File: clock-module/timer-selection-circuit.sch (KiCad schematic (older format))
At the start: 15 parts

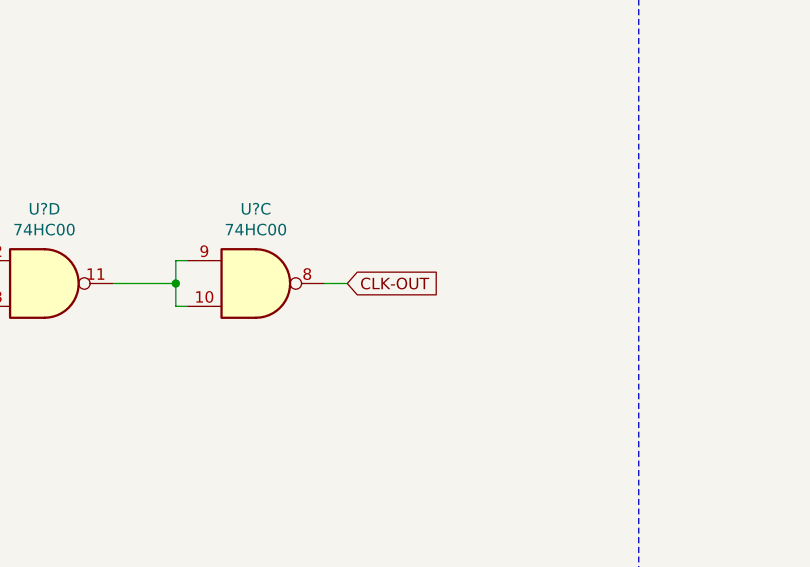
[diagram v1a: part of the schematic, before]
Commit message: Add clock inverter to clock-module, correct label directions
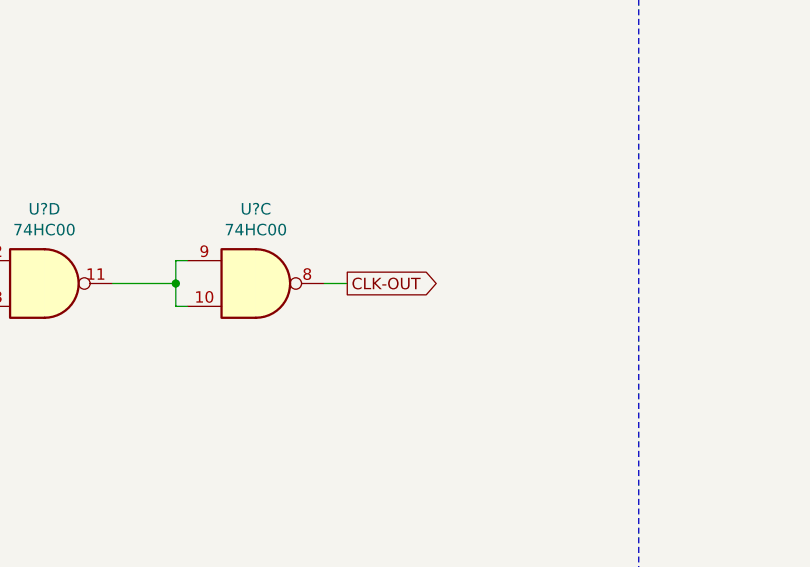
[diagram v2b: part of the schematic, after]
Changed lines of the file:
@@
 Text Notes 625  700  0    79   ~ 16
 Timer Selection Circuit
-Text GLabel 5700 2575 2    50   Input ~ 0
+Text GLabel 5700 2575 2    50   Output ~ 0
 CLK-OUT
 Wire Wire Line

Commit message: ERC complete on clock-module, add HLT connector
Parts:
- gave numbers to parts that had none: 7
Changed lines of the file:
@@
 	5000 2475 4950 2475
 $Comp
-L 74xx:74HC00 U?
+L 74xx:74HC00 U4
 U 3 1 5D440F0A
 P 5300 2575
-AR Path="/5D28C6D7/5D440F0A" Ref="U?"  Part="3"
+AR Path="/5D28C6D7/5D440F0A" Ref="U4"  Part="3"
 AR Path="/5D440F0A" Ref="U?"  Part="3"
-F 0 "U?" H 5300 2900 50  0000 C CNN
+F 0 "U4" H 5300 2900 50  0000 C CNN
 F 1 "74HC00" H 5300 2809 50  0000 C CNN
 F 2 "" H 5300 2575 50  0001 C CNN
@@
 $EndComp
 $Comp
-L 74xx:74HC00 U?
+L 74xx:74HC00 U4
 U 4 1 5D440F10
 P 4375 2575
-AR Path="/5D28C6D7/5D440F10" Ref="U?"  Part="4"
+AR Path="/5D28C6D7/5D440F10" Ref="U4"  Part="4"
 AR Path="/5D440F10" Ref="U?"  Part="4"
-F 0 "U?" H 4375 2900 50  0000 C CNN
+F 0 "U4" H 4375 2900 50  0000 C CNN
 F 1 "74HC00" H 4375 2809 50  0000 C CNN
 F 2 "" H 4375 2575 50  0001 C CNN
@@
 $EndComp
 $Comp
-L 74xx:74HC00 U?
+L 74xx:74HC00 U3
 U 2 1 5D440F16
 P 3575 2200
-AR Path="/5D28C6D7/5D440F16" Ref="U?"  Part="2"
+AR Path="/5D28C6D7/5D440F16" Ref="U3"  Part="2"
 AR Path="/5D440F16" Ref="U?"  Part="2"
-F 0 "U?" H 3575 2525 50  0000 C CNN
+F 0 "U3" H 3575 2525 50  0000 C CNN
 F 1 "74HC00" H 3575 2434 50  0000 C CNN
 F 2 "" H 3575 2200 50  0001 C CNN
@@
 $EndComp
 $Comp
-L 74xx:74HC00 U?
+L 74xx:74HC00 U3
 U 1 1 5D440F1C
 P 3550 2950
-AR Path="/5D28C6D7/5D440F1C" Ref="U?"  Part="1"
+AR Path="/5D28C6D7/5D440F1C" Ref="U3"  Part="1"
 AR Path="/5D440F1C" Ref="U?"  Part="1"
-F 0 "U?" H 3550 2725 50  0000 C CNN
+F 0 "U3" H 3550 2725 50  0000 C CNN
 F 1 "74HC00" H 3550 2625 50  0000 C CNN
 F 2 "" H 3550 2950 50  0001 C CNN
@@
 SWITCH-Q
 $Comp
-L 74xx:74HC00 U?
+L 74xx:74HC00 U3
 U 4 1 5D440F28
 P 2550 1900
-AR Path="/5D28C6D7/5D440F28" Ref="U?"  Part="4"
+AR Path="/5D28C6D7/5D440F28" Ref="U3"  Part="4"
 AR Path="/5D440F28" Ref="U?"  Part="4"
-F 0 "U?" H 2550 2225 50  0000 C CNN
+F 0 "U3" H 2550 2225 50  0000 C CNN
 F 1 "74HC00" H 2550 2134 50  0000 C CNN
 F 2 "" H 2550 1900 50  0001 C CNN
@@
 $EndComp
 $Comp
-L 74xx:74HC00 U?
+L 74xx:74HC00 U3
 U 3 1 5D440F2E
 P 2550 2500
-AR Path="/5D28C6D7/5D440F2E" Ref="U?"  Part="3"
+AR Path="/5D28C6D7/5D440F2E" Ref="U3"  Part="3"
 AR Path="/5D440F2E" Ref="U?"  Part="3"
-F 0 "U?" H 2550 2825 50  0000 C CNN
+F 0 "U3" H 2550 2825 50  0000 C CNN
 F 1 "74HC00" H 2550 2734 50  0000 C CNN
 F 2 "" H 2550 2500 50  0001 C CNN
@@
 P 2850 5300
 AR Path="/5D446D25" Ref="R?"  Part="1"
-AR Path="/5D28C6D7/5D446D25" Ref="R?"  Part="1"
-F 0 "R?" H 2920 5346 50  0000 L CNN
+AR Path="/5D28C6D7/5D446D25" Ref="R8"  Part="1"
+F 0 "R8" H 2920 5346 50  0000 L CNN
 F 1 "R" H 2920 5255 50  0000 L CNN
 F 2 "" V 2780 5300 50  0001 C CNN
@@
 P 2850 6375
 AR Path="/5D446D2B" Ref="R?"  Part="1"
-AR Path="/5D28C6D7/5D446D2B" Ref="R?"  Part="1"
-F 0 "R?" H 2920 6421 50  0000 L CNN
+AR Path="/5D28C6D7/5D446D2B" Ref="R9"  Part="1"
+F 0 "R9" H 2920 6421 50  0000 L CNN
 F 1 "R" H 2920 6330 50  0000 L CNN
 F 2 "" V 2780 6375 50  0001 C CNN
@@
 P 2650 5825
 AR Path="/5D446D31" Ref="SW?"  Part="1"
-AR Path="/5D28C6D7/5D446D31" Ref="SW?"  Part="1"
-F 0 "SW?" H 2250 5400 50  0000 C CNN
+AR Path="/5D28C6D7/5D446D31" Ref="SW2"  Part="1"
+F 0 "SW2" H 2250 5400 50  0000 C CNN
 F 1 "SW_SPDT" H 2400 5600 50  0000 C CNN
 F 2 "" H 2650 5825 50  0001 C CNN
@@
 	4475 5550 4975 5550
 $Comp
-L power:GND #PWR?
+L power:GND #PWR0128
 U 1 1 5D446D3C
 P 2275 5950
-AR Path="/5D28C6D7/5D446D3C" Ref="#PWR?"  Part="1"
+AR Path="/5D28C6D7/5D446D3C" Ref="#PWR0128"  Part="1"
 AR Path="/5D446D3C" Ref="#PWR?"  Part="1"
-F 0 "#PWR?" H 2275 5700 50  0001 C CNN
+F 0 "#PWR0128" H 2275 5700 50  0001 C CNN
 F 1 "GND" H 2280 5777 50  0000 C CNN
 F 2 "" H 2275 5950 50  0001 C CNN
@@
 	2275 5800 2450 5825
 $Comp
-L power:+5V #PWR?
+L power:+5V #PWR0129
 U 1 1 5D446D44
 P 2850 5100
-AR Path="/5D28C6D7/5D446D44" Ref="#PWR?"  Part="1"
+AR Path="/5D28C6D7/5D446D44" Ref="#PWR0129"  Part="1"
 AR Path="/5D446D44" Ref="#PWR?"  Part="1"
-F 0 "#PWR?" H 2850 4950 50  0001 C CNN
+F 0 "#PWR0129" H 2850 4950 50  0001 C CNN
 F 1 "+5V" H 2865 5273 50  0000 C CNN
 F 2 "" H 2850 5100 50  0001 C CNN
@@
 	2850 5100 2850 5150
 $Comp
-L power:+5V #PWR?
+L power:+5V #PWR0130
 U 1 1 5D446D4B
 P 2850 6600
-AR Path="/5D28C6D7/5D446D4B" Ref="#PWR?"  Part="1"
+AR Path="/5D28C6D7/5D446D4B" Ref="#PWR0130"  Part="1"
 AR Path="/5D446D4B" Ref="#PWR?"  Part="1"
-F 0 "#PWR?" H 2850 6450 50  0001 C CNN
+F 0 "#PWR0130" H 2850 6450 50  0001 C CNN
 F 1 "+5V" H 2865 6773 50  0000 C CNN
 F 2 "" H 2850 6600 50  0001 C CNN
@@
 	3350 6025 3875 6025
 $Comp
-L 74xx:74HC00 U?
+L 74xx:74HC00 U4
 U 2 1 5D446D55
 P 4175 5550
-AR Path="/5D28C6D7/5D446D55" Ref="U?"  Part="2"
+AR Path="/5D28C6D7/5D446D55" Ref="U4"  Part="2"
 AR Path="/5D446D55" Ref="U?"  Part="2"
-F 0 "U?" H 4175 5875 50  0000 C CNN
+F 0 "U4" H 4175 5875 50  0000 C CNN
 F 1 "74HC00" H 4175 5784 50  0000 C CNN
 F 2 "" H 4175 5550 50  0001 C CNN
@@
 $EndComp
 $Comp
-L 74xx:74HC00 U?
+L 74xx:74HC00 U4
 U 1 1 5D446D5B
 P 4175 6125
-AR Path="/5D28C6D7/5D446D5B" Ref="U?"  Part="1"
+AR Path="/5D28C6D7/5D446D5B" Ref="U4"  Part="1"
 AR Path="/5D446D5B" Ref="U?"  Part="1"
-F 0 "U?" H 4175 5925 50  0000 C CNN
+F 0 "U4" H 4175 5925 50  0000 C CNN
 F 1 "74HC00" H 4175 5850 50  0000 C CNN
 F 2 "" H 4175 6125 50  0001 C CNN
@@
 	2850 6100 2850 6225
 $Comp
-L 74xx:74HC00 U?
+L 74xx:74HC00 U4
 U 5 1 5D450474
 P 9650 2525
-AR Path="/5D28C6D7/5D450474" Ref="U?"  Part="5"
+AR Path="/5D28C6D7/5D450474" Ref="U4"  Part="5"
 AR Path="/5D450474" Ref="U?"  Part="5"
-F 0 "U?" H 9880 2571 50  0000 L CNN
+F 0 "U4" H 9880 2571 50  0000 L CNN
 F 1 "74HC00" H 9880 2480 50  0000 L CNN
 F 2 "" H 9650 2525 50  0001 C CNN
@@
 $EndComp
 $Comp
-L 74xx:74HC00 U?
+L 74xx:74HC00 U3
 U 5 1 5D45047A
 P 8475 2525
-AR Path="/5D28C6D7/5D45047A" Ref="U?"  Part="5"
+AR Path="/5D28C6D7/5D45047A" Ref="U3"  Part="5"
 AR Path="/5D45047A" Ref="U?"  Part="5"
-F 0 "U?" H 8705 2571 50  0000 L CNN
+F 0 "U3" H 8705 2571 50  0000 L CNN
 F 1 "74HC00" H 8705 2480 50  0000 L CNN
 F 2 "" H 8475 2525 50  0001 C CNN
@@
 $EndComp
 $Comp
-L power:+5V #PWR?
+L power:+5V #PWR0131
 U 1 1 5D450480
 P 8475 1900
-AR Path="/5D28C6D7/5D450480" Ref="#PWR?"  Part="1"
+AR Path="/5D28C6D7/5D450480" Ref="#PWR0131"  Part="1"
 AR Path="/5D450480" Ref="#PWR?"  Part="1"
-F 0 "#PWR?" H 8475 1750 50  0001 C CNN
+F 0 "#PWR0131" H 8475 1750 50  0001 C CNN
 F 1 "+5V" H 8490 2073 50  0000 C CNN
 F 2 "" H 8475 1900 50  0001 C CNN
@@
 $EndComp
 $Comp
-L power:+5V #PWR?
+L power:+5V #PWR0132
 U 1 1 5D450486
 P 9650 1900
-AR Path="/5D28C6D7/5D450486" Ref="#PWR?"  Part="1"
+AR Path="/5D28C6D7/5D450486" Ref="#PWR0132"  Part="1"
 AR Path="/5D450486" Ref="#PWR?"  Part="1"
-F 0 "#PWR?" H 9650 1750 50  0001 C CNN
+F 0 "#PWR0132" H 9650 1750 50  0001 C CNN
 F 1 "+5V" H 9665 2073 50  0000 C CNN
 F 2 "" H 9650 1900 50  0001 C CNN
@@
 $EndComp
 $Comp
-L power:GND #PWR?
+L power:GND #PWR0133
 U 1 1 5D45048C
 P 8475 3150
-AR Path="/5D28C6D7/5D45048C" Ref="#PWR?"  Part="1"
+AR Path="/5D28C6D7/5D45048C" Ref="#PWR0133"  Part="1"
 AR Path="/5D45048C" Ref="#PWR?"  Part="1"
-F 0 "#PWR?" H 8475 2900 50  0001 C CNN
+F 0 "#PWR0133" H 8475 2900 50  0001 C CNN
 F 1 "GND" H 8480 2977 50  0000 C CNN
 F 2 "" H 8475 3150 50  0001 C CNN
@@
 $EndComp
 $Comp
-L power:GND #PWR?
+L power:GND #PWR0134
 U 1 1 5D450492
 P 9650 3150
-AR Path="/5D28C6D7/5D450492" Ref="#PWR?"  Part="1"
+AR Path="/5D28C6D7/5D450492" Ref="#PWR0134"  Part="1"
 AR Path="/5D450492" Ref="#PWR?"  Part="1"
-F 0 "#PWR?" H 9650 2900 50  0001 C CNN
+F 0 "#PWR0134" H 9650 2900 50  0001 C CNN
 F 1 "GND" H 9655 2977 50  0000 C CNN
 F 2 "" H 9650 3150 50  0001 C CNN
@@
 	9650 2025 9650 1900
 $Comp
-L Device:C C?
+L Device:C C9
 U 1 1 5D45049C
 P 7900 1700
-AR Path="/5D28C6D7/5D45049C" Ref="C?"  Part="1"
+AR Path="/5D28C6D7/5D45049C" Ref="C9"  Part="1"
 AR Path="/5D45049C" Ref="C?"  Part="1"
-F 0 "C?" H 8015 1746 50  0000 L CNN
+F 0 "C9" H 8015 1746 50  0000 L CNN
 F 1 "C" H 8015 1655 50  0000 L CNN
 F 2 "" H 7938 1550 50  0001 C CNN
@@
 $EndComp
 $Comp
-L power:+5V #PWR?
+L power:+5V #PWR0135
 U 1 1 5D4504A2
 P 7900 1425
-AR Path="/5D28C6D7/5D4504A2" Ref="#PWR?"  Part="1"
+AR Path="/5D28C6D7/5D4504A2" Ref="#PWR0135"  Part="1"
 AR Path="/5D4504A2" Ref="#PWR?"  Part="1"
-F 0 "#PWR?" H 7900 1275 50  0001 C CNN
+F 0 "#PWR0135" H 7900 1275 50  0001 C CNN
 F 1 "+5V" H 7915 1598 50  0000 C CNN
 F 2 "" H 7900 1425 50  0001 C CNN
@@
 $EndComp
 $Comp
-L power:GND #PWR?
+L power:GND #PWR0136
 U 1 1 5D4504A8
 P 7900 1975
-AR Path="/5D28C6D7/5D4504A8" Ref="#PWR?"  Part="1"
+AR Path="/5D28C6D7/5D4504A8" Ref="#PWR0136"  Part="1"
 AR Path="/5D4504A8" Ref="#PWR?"  Part="1"
-F 0 "#PWR?" H 7900 1725 50  0001 C CNN
+F 0 "#PWR0136" H 7900 1725 50  0001 C CNN
 F 1 "GND" H 7905 1802 50  0000 C CNN
 F 2 "" H 7900 1975 50  0001 C CNN
@@
 	7900 1550 7900 1425
 $Comp
-L Device:C C?
+L Device:C C10
 U 1 1 5D4504B0
 P 10225 1700
-AR Path="/5D28C6D7/5D4504B0" Ref="C?"  Part="1"
+AR Path="/5D28C6D7/5D4504B0" Ref="C10"  Part="1"
 AR Path="/5D4504B0" Ref="C?"  Part="1"
-F 0 "C?" H 10340 1746 50  0000 L CNN
+F 0 "C10" H 10340 1746 50  0000 L CNN
 F 1 "C" H 10340 1655 50  0000 L CNN
 F 2 "" H 10263 1550 50  0001 C CNN
@@
 $EndComp
 $Comp
-L power:+5V #PWR?
+L power:+5V #PWR0137
 U 1 1 5D4504B6
 P 10225 1425
-AR Path="/5D28C6D7/5D4504B6" Ref="#PWR?"  Part="1"
+AR Path="/5D28C6D7/5D4504B6" Ref="#PWR0137"  Part="1"
 AR Path="/5D4504B6" Ref="#PWR?"  Part="1"
-F 0 "#PWR?" H 10225 1275 50  0001 C CNN
+F 0 "#PWR0137" H 10225 1275 50  0001 C CNN
 F 1 "+5V" H 10240 1598 50  0000 C CNN
 F 2 "" H 10225 1425 50  0001 C CNN
@@
 $EndComp
 $Comp
-L power:GND #PWR?
+L power:GND #PWR0138
 U 1 1 5D4504BC
 P 10225 1975
-AR Path="/5D28C6D7/5D4504BC" Ref="#PWR?"  Part="1"
+AR Path="/5D28C6D7/5D4504BC" Ref="#PWR0138"  Part="1"
 AR Path="/5D4504BC" Ref="#PWR?"  Part="1"
-F 0 "#PWR?" H 10225 1725 50  0001 C CNN
+F 0 "#PWR0138" H 10225 1725 50  0001 C CNN
 F 1 "GND" H 10230 1802 50  0000 C CNN
 F 2 "" H 10225 1975 50  0001 C CNN
